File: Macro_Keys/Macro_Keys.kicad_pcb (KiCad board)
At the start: 2 copper layers, 100 x 100 mm, 47 parts, among them J1 USB_C_Receptacle_USB2.0, J2 ICSP, J3 OLED, SW1 RST, SW10 SW, SW11 SW, SW12 SW, SW13 SW, SW14 SW, SW15 SW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

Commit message: working on layout
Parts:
- removed SW12, SW13, SW14, SW15, SW16, SW17: SW, Button_Switch_Keyboard:SW_Cherry_MX_1.00u_PCB
- removed SW18: Mode, Button_Switch_THT:SW_PUSH_6mm
- added R2: 1M, Resistor_SMD:R_0805_2012Metric, B.Cu at (53.0, 15.0)
- added R5: 10K, Resistor_SMD:R_0805_2012Metric, F.Cu at (31.0, 31.0)
- C10: value 100nF -> 10uF; footprint Capacitor_SMD:C_0805_2012Metric -> Capacitor_SMD:CP_Elec_4x5.4
- C11: value 100nF -> 1uF; moved to F.Cu
- C3, R1, R3, R4, Y1: moved to F.Cu
- C5, C6: value 22pF -> 100nF; moved to F.Cu
- C7: value 100nF -> 22pF; moved to F.Cu
- C8: value 10uF -> 22pF; footprint Capacitor_SMD:CP_Elec_4x5.4 -> Capacitor_SMD:C_0805_2012Metric
- C9: value 1uF -> 100nF; moved to F.Cu
- J1: value USB_C_Receptacle_USB2.0 -> ICSP; footprint Connector_USB:USB_C_Receptacle_HRO_TYPE-C-31-M-12 -> Custom_Vertical_2x_2.54mm_Pin_Header:PinHeader_2x03_P2.54mm_Vertical
- J2: value ICSP -> OLED; footprint Custom_Vertical_2x_2.54mm_Pin_Header:PinHeader_2x03_P2.54mm_Vertical -> Custom_Vertical_1x_2.54mm_Pin_Header:PinHeader_1x04_P2.54mm_Vertical
- J3: value OLED -> USB_C_Receptacle_USB2.0; footprint Custom_Vertical_1x_2.54mm_Pin_Header:PinHeader_1x04_P2.54mm_Vertical -> Connector_USB:USB_C_Receptacle_HRO_TYPE-C-31-M-12
- R6: value 10K -> 0R
- SW11: value SW -> Mode; footprint Button_Switch_Keyboard:SW_Cherry_MX_1.00u_PCB -> Button_Switch_THT:SW_PUSH_6mm
- U1: value ATmega32U4-AU -> ME6212; footprint Package_QFP:TQFP-44_10x10mm_P0.8mm -> Package_TO_SOT_SMD:SOT-23-5
- U2: value AMS1117-5.0 -> ATmega32U4-AU; footprint Package_TO_SOT_SMD:SOT-223-3_TabPin2 -> Package_QFP:TQFP-44_10x10mm_P0.8mm
- moved D3 63.5 mm to (107.0, 45.0), turned to 0 degrees
- moved J3 61.8 mm to (91.0, 15.0), turned to 180 degrees
- moved D4 61.4 mm to (107.0, 49.0)
- moved D2 60.2 mm to (107.0, 41.0), turned to 0 degrees
- moved R6 56.8 mm to (71.4, 20.5), turned to -90 degrees
- moved SW11 49.9 mm to (21.0, 30.0)
- moved SW5 47.3 mm to (45.3, 56.9)
- moved SW10 43.3 mm to (83.7, 76.1)
- moved R1 40.5 mm to (101.0, 37.0), turned to -90 degrees
- moved SW1 38.0 mm to (107.0, 34.0), turned to 0 degrees
- moved SW8 37.7 mm to (45.3, 76.1)
- moved C8 37.3 mm to (64.5, 15.5), turned to -90 degrees
- moved SW9 34.8 mm to (64.5, 76.1)
- moved C9 32.1 mm to (94.0, 39.0), turned to 0 degrees
- moved D1 30.4 mm to (106.9, 53.0)
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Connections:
- C1 pad 1: +5V -> VBUS
- C10 pad 1: VBUS -> GNDREF
- C10 pad 2: GNDREF -> VBUS
- C11 pad 1: +5V -> Net-(C11-Pad1)
- C5 pad 1: Net-(C5-Pad1) -> +5V
- C6 pad 1: Net-(C6-Pad1) -> +5V
- C8 pad 1: GNDREF -> Net-(C8-Pad1)
- C8 pad 2: VBUS -> GNDREF
- J2 pad 1: /MISO -> /D2
- J2 pad 2: +5V -> /D3
- J2 pad 3: /SCK -> +5V
- J2 pad 4: /MOSI -> GNDREF
- R6 pad 1: Net-(R1-Pad1) -> VBUS
- R6 pad 2: +5V -> Net-(R6-Pad2)
- SW10 pad 2: /C0 -> /C2
- SW11 pad 1: /A2 -> /A5
- SW11 pad 2: /C1 -> +5V
- SW5 pad 1: /A0 -> /A1
- SW5 pad 2: /C3 -> /C0
- SW6 pad 2: /C0 -> /C1
- SW7 pad 2: /C1 -> /C2
- SW8 pad 1: /A1 -> /A2
- SW8 pad 2: /C2 -> /C0
- SW9 pad 1: /A1 -> /A2
- SW9 pad 2: /C3 -> /C1
- U1 pad 1: /D7 -> VBUS
- U1 pad 2: +5V -> GNDREF
- U1 pad 3: /D- -> VBUS
- U1 pad 4: /D+ -> Net-(U1-Pad4)
- U1 pad 5: GNDREF -> +5V
- U2 pad 1: GNDREF -> /D7
- U2 pad 3: VBUS -> /D-
- Y1 pad 1: Net-(C6-Pad1) -> Net-(C8-Pad1)
- Y1 pad 3: Net-(C5-Pad1) -> Net-(C7-Pad1)
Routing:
- net /A3: track 100.1 -> 0.00 mm, vias 4 -> 0
- net /C3: track 82.1 -> 0.00 mm
- net /RST: track 44.7 -> 0.00 mm, vias 1 -> 0
- net /D-: track 35.8 -> 0.00 mm
- net /MISO: track 35.7 -> 0.00 mm, vias 1 -> 0
- net /MOSI: track 33.6 -> 0.00 mm, vias 1 -> 0
- net /D+: track 32.7 -> 0.00 mm
- net /SCK: track 31.5 -> 0.00 mm, vias 1 -> 0
- net /RXLED: track 17.5 -> 0.00 mm, vias 2 -> 0
- net VBUS: track 18.9 -> 32.4 mm
- net /C0: track 72.3 -> 61.0 mm
- net /C2: track 69.9 -> 79.5 mm
- net /A2: track 82.5 -> 91.9 mm, vias 5 -> 2
- net Net-(C6-Pad1): track 8.79 -> 0.00 mm, vias 1 -> 0
- net +5V: track 8.75 -> 0.00 mm, vias 2 -> 0
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- removed copper zone on F.Cu, net GNDREF
- removed copper zone on F.Cu, net VBUS
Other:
- net class Default removed

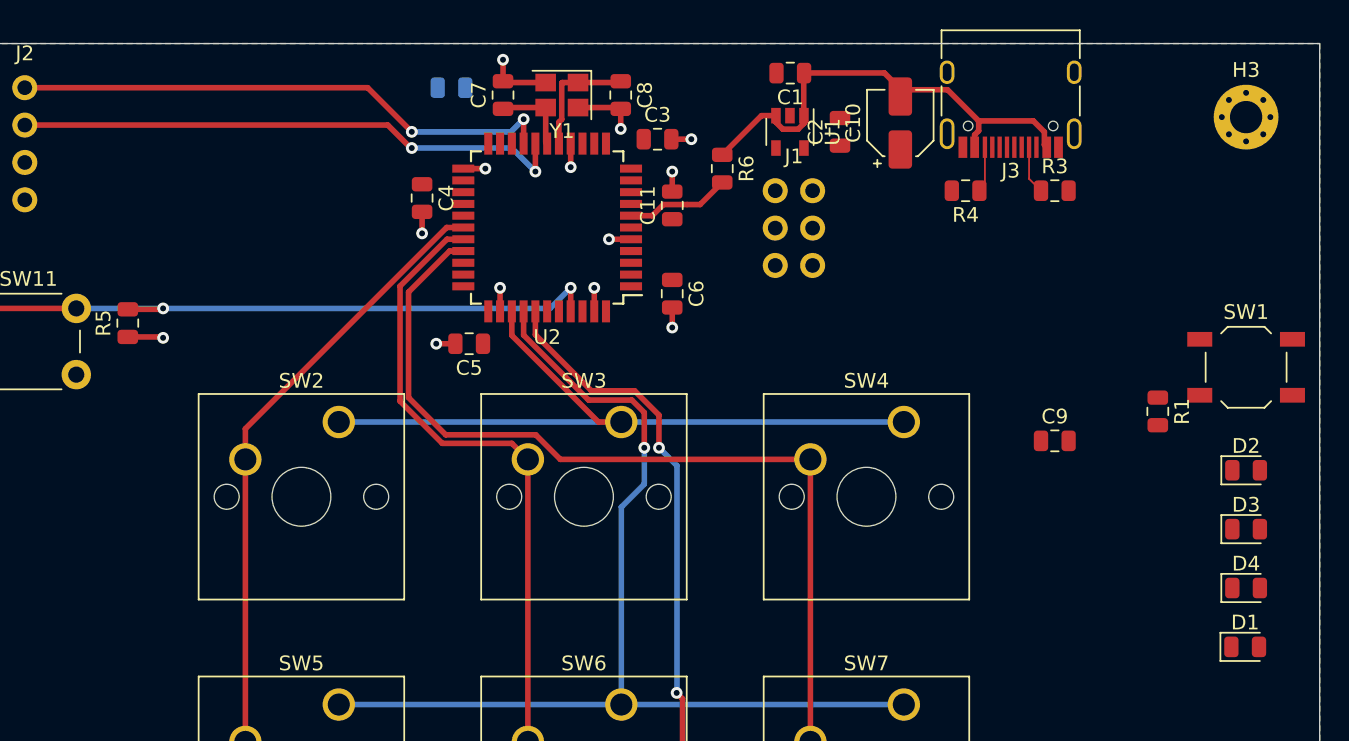
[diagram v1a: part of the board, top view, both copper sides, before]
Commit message: Macro_Keys Layout complete + Programmer WIP
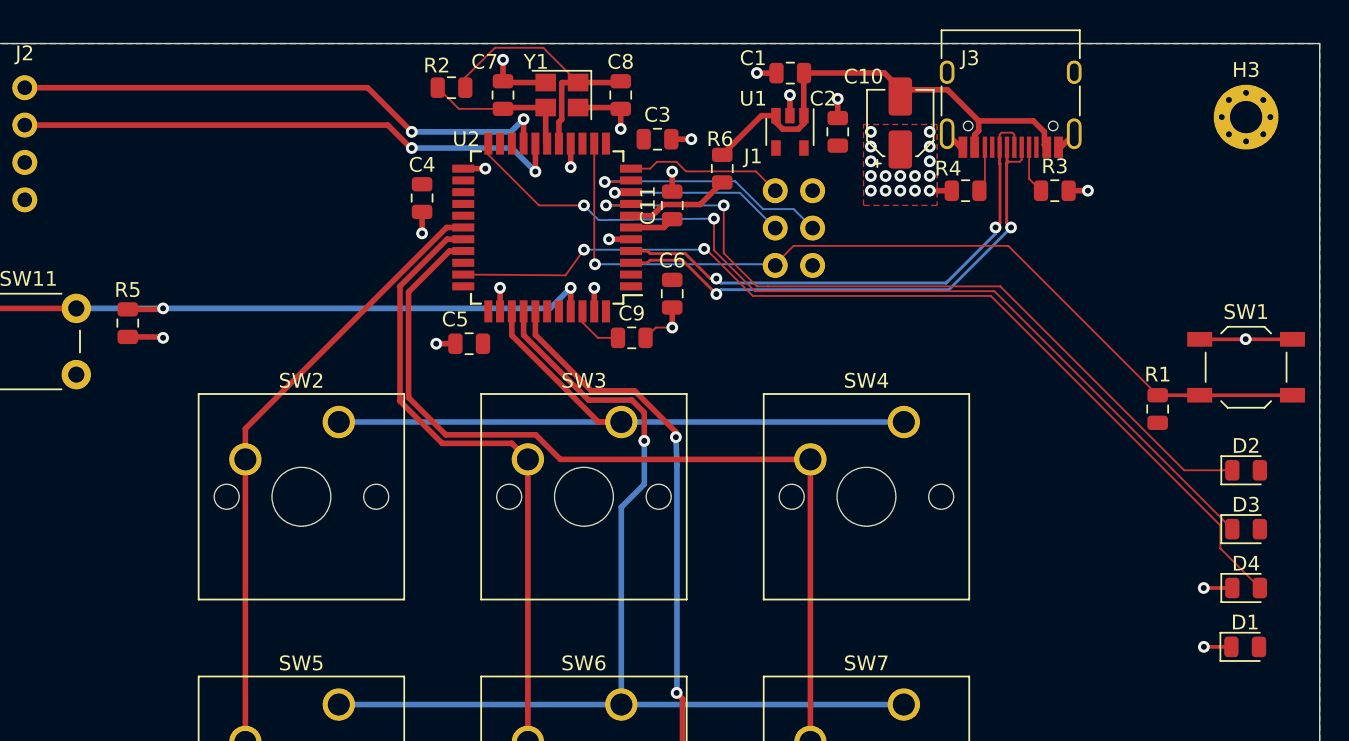
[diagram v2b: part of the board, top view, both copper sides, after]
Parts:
- R2: moved to F.Cu
- moved C9 29.6 mm to (65.2, 32.0)
- moved R1 0.16 mm to (101.0, 36.8)
- moved C2 0.15 mm to (79.2, 18.0)
- turned R2 to 180 degrees
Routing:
- net /IO13: track 0.00 -> 65.5 mm, vias 0 -> 2
- net /TXLED: track 0.00 -> 63.2 mm, vias 0 -> 2
- net /RST: track 0.00 -> 60.5 mm, vias 0 -> 1
- net /RXLED: track 0.00 -> 53.7 mm, vias 0 -> 2
- net /D-: track 0.00 -> 37.1 mm, vias 0 -> 2
- net /D+: track 0.00 -> 35.9 mm, vias 0 -> 2
- net GNDREF: track 25.8 -> 47.8 mm, vias 13 -> 36
- net /MOSI: track 0.00 -> 17.3 mm, vias 0 -> 1
- net /SCK: track 0.00 -> 13.0 mm, vias 0 -> 1
- net /MISO: track 0.00 -> 10.8 mm
- net Net-(C8-Pad1): track 8.26 -> 18.4 mm
- net Net-(C7-Pad1): track 5.43 -> 10.5 mm
- net Net-(C9-Pad1): track 0.00 -> 3.60 mm
- net Net-(C11-Pad1): track 0.00 -> 3.03 mm
- added copper zone on F.Cu, net GNDREF
